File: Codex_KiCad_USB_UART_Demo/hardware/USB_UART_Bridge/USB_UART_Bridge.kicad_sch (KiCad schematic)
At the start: 8 parts, among them J1 USB-C_Receptacle_USB2.0, J2 UART, U2 USBLC6-2SC6

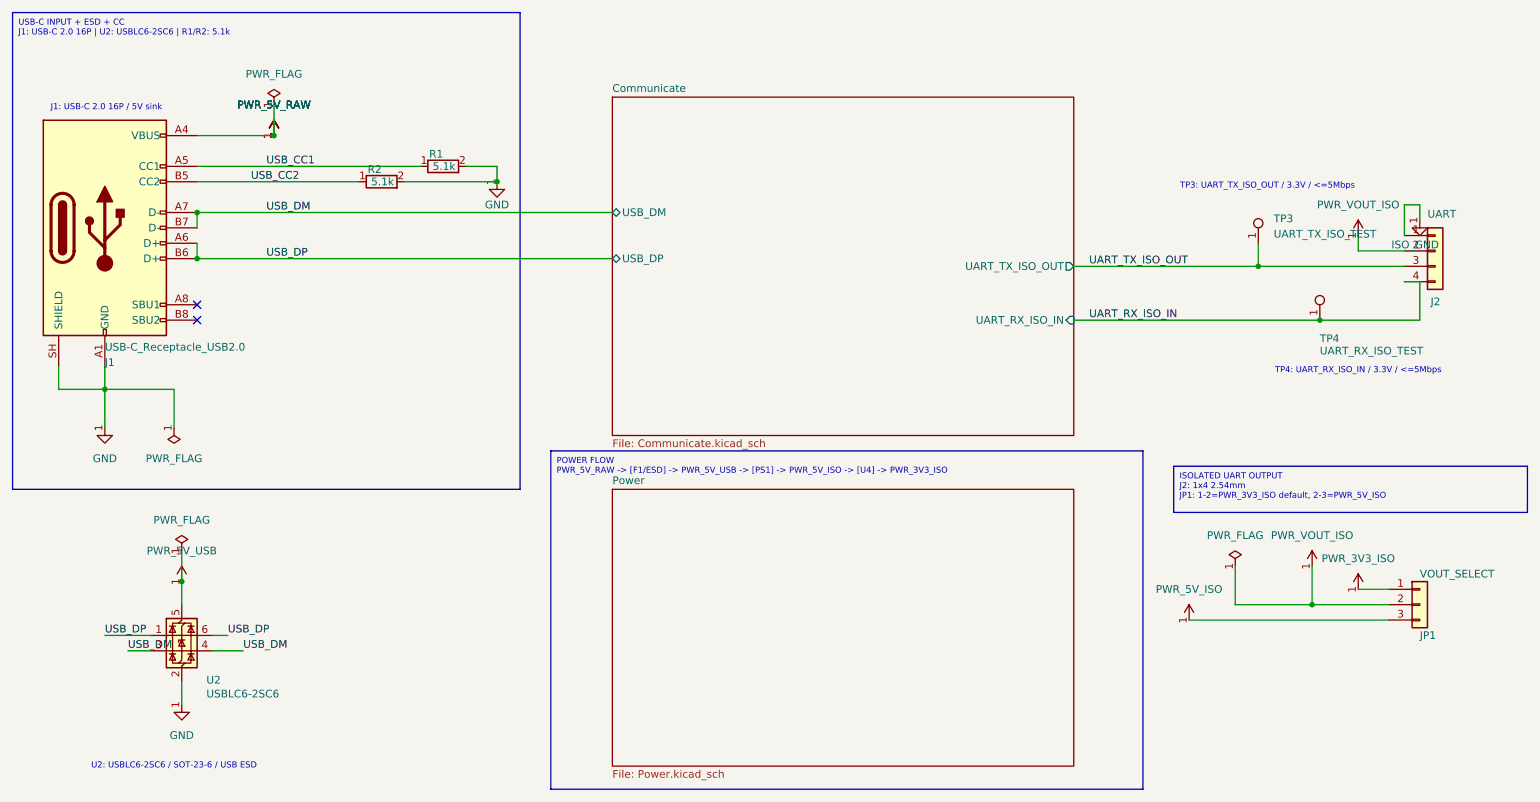
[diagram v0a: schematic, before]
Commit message: feat: complete USB UART PCB layout and routing
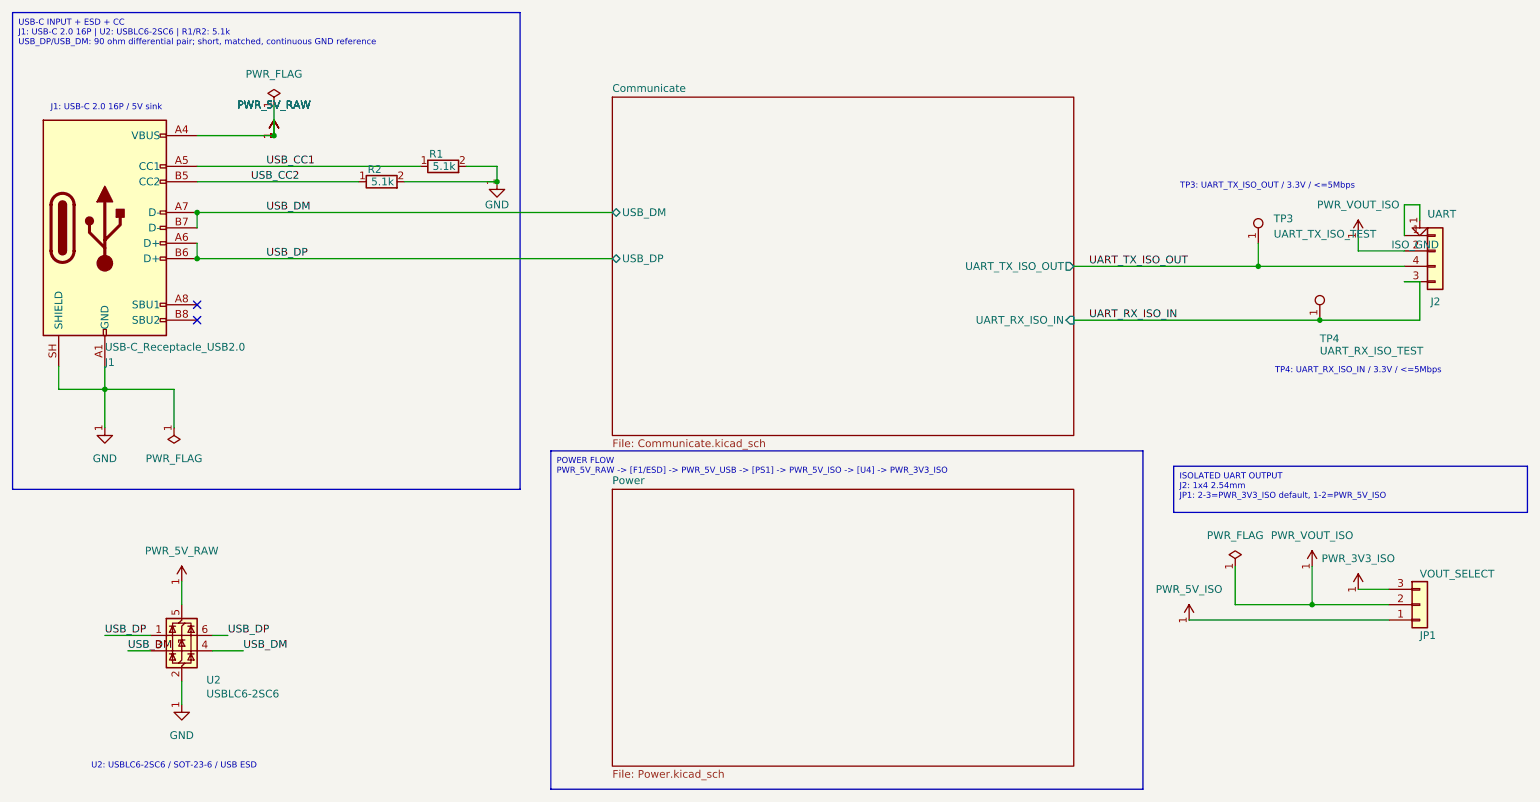
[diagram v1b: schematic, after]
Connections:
- net PWR_5V_USB is gone; now on net PWR_5V_RAW: U2.5 (VBUS)
- net PWR_3V3_ISO: now also JP1.3 (Pin_3); no longer JP1.1 (Pin_1)
- net PWR_5V_ISO: now also JP1.1 (Pin_1); no longer JP1.3 (Pin_3)
- net UART_RX_ISO_IN: now also J2.3 (Pin_3); no longer J2.4 (Pin_4)
- net UART_TX_ISO_OUT: now also J2.4 (Pin_4); no longer J2.3 (Pin_3)
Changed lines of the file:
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@@
 	(title_block
 		(title "USB_UART_Bridge")
+		(date "2026-09-19")
 		(rev "0.2")
-		(date "2026-09-19")
 	)
 	(text "TP3: UART_TX_ISO_OUT / 3.3V / <=5Mbps"
@@
 		)
 	)
-	(text_box "ISOLATED UART OUTPUT\nJ2: 1x4 2.54mm\nJP1: 1-2=PWR_3V3_ISO default, 2-3=PWR_5V_ISO"
+	(text_box "ISOLATED UART OUTPUT\nJ2: 1x4 2.54mm\nJP1: 2-3=PWR_3V3_ISO default, 1-2=PWR_5V_ISO"
 		(exclude_from_sim no)
 		(at 217.17 106.68 0)
@@
 		)
 	)
-	(text_box "USB-C INPUT + ESD + CC\nJ1: USB-C 2.0 16P | U2: USBLC6-2SC6 | R1/R2: 5.1k"
+	(text_box "USB-C INPUT + ESD + CC\nJ1: USB-C 2.0 16P | U2: USBLC6-2SC6 | R1/R2: 5.1k\nUSB_DP/USB_DM: 90 ohm differential pair; short, matched, continuous GND reference"
 		(exclude_from_sim no)
 		(at 25.4 31.75 0)
@@
 	)
 	(junction
-		(at 53.34 125.73)
-		(diameter 0)
-		(color 0 0 0 0)
-	)
-	(junction
 		(at 231.14 73.66)
 		(diameter 0)
@@
 		(pts
 			(xy 100.33 57.15) (xy 105.41 57.15)
-		)
-		(stroke
-			(width 0)
-			(type default)
-		)
-	)
-	(wire
-		(pts
-			(xy 53.34 125.73) (xy 53.34 120.65)
 		)
 		(stroke
@@
 		(instances
 			(project "USB_UART_Bridge"
-				(path "/6d719abe-8294-4a13-afeb-1c2f95178f03"
+				(path "/991ad087-5b84-4353-b5af-12ada82ec90c"
 					(reference "#PWR055")
 					(unit 1)
@@
 		(instances
 			(project "USB_UART_Bridge"
-				(path "/6d719abe-8294-4a13-afeb-1c2f95178f03"
+				(path "/991ad087-5b84-4353-b5af-12ada82ec90c"
 					(reference "#PWR047")
 					(unit 1)
@@
 		(instances
 			(project "USB_UART_Bridge"
-				(path "/6d719abe-8294-4a13-afeb-1c2f95178f03"
+				(path "/991ad087-5b84-4353-b5af-12ada82ec90c"
 					(reference "#PWR046")
 					(unit 1)
@@
 		(instances
 			(project "USB_UART_Bridge"
-				(path "/6d719abe-8294-4a13-afeb-1c2f95178f03"
+				(path "/991ad087-5b84-4353-b5af-12ada82ec90c"
 					(reference "#PWR048")
 					(unit 1)
@@
 		(instances
 			(project "USB_UART_Bridge"
-				(path "/6d719abe-8294-4a13-afeb-1c2f95178f03"
+				(path "/991ad087-5b84-4353-b5af-12ada82ec90c"
 					(reference "#FLG004")
 					(unit 1)
@@
 		(instances
 			(project "USB_UART_Bridge"
-				(path "/6d719abe-8294-4a13-afeb-1c2f95178f03"
+				(path "/991ad087-5b84-4353-b5af-12ada82ec90c"
 					(reference "U2")
 					(unit 1)
@@
 		(instances
 			(project "USB_UART_Bridge"
-				(path "/6d719abe-8294-4a13-afeb-1c2f95178f03"
+				(path "/991ad087-5b84-4353-b5af-12ada82ec90c"
 					(reference "#PWR059")
 					(unit 1)
@@
 		(instances
 			(project "USB_UART_Bridge"
-				(path "/6d719abe-8294-4a13-afeb-1c2f95178f03"
+				(path "/991ad087-5b84-4353-b5af-12ada82ec90c"
 					(reference "#PWR058")
 					(unit 1)
@@
 		(instances
 			(project "USB_UART_Bridge"
-				(path "/6d719abe-8294-4a13-afeb-1c2f95178f03"
+				(path "/991ad087-5b84-4353-b5af-12ada82ec90c"
 					(reference "#FLG003")
 					(unit 1)
@@
 		(instances
 			(project "USB_UART_Bridge"
-				(path "/6d719abe-8294-4a13-afeb-1c2f95178f03"
+				(path "/991ad087-5b84-4353-b5af-12ada82ec90c"
 					(reference "#PWR060")
 					(unit 1)
@@
 		(instances
 			(project "USB_UART_Bridge"
-				(path "/6d719abe-8294-4a13-afeb-1c2f95178f03"
+				(path "/991ad087-5b84-4353-b5af-12ada82ec90c"
 					(reference "#PWR062")
 					(unit 1)
@@
 		(instances
 			(project "USB_UART_Bridge"
-				(path "/6d719abe-8294-4a13-afeb-1c2f95178f03"
+				(path "/991ad087-5b84-4353-b5af-12ada82ec90c"
 					(reference "#PWR052")
 					(unit 1)
@@
 		(instances
 			(project "USB_UART_Bridge"
-				(path "/6d719abe-8294-4a13-afeb-1c2f95178f03"
+				(path "/991ad087-5b84-4353-b5af-12ada82ec90c"
 					(reference "#PWR061")
 					(unit 1)
@@
 		(instances
 			(project "USB_UART_Bridge"
-				(path "/6d719abe-8294-4a13-afeb-1c2f95178f03"
+				(path "/991ad087-5b84-4353-b5af-12ada82ec90c"
 					(reference "J1")
 					(unit 1)
@@
 		(instances
 			(project "USB_UART_Bridge"
-				(path "/6d719abe-8294-4a13-afeb-1c2f95178f03"
+				(path "/991ad087-5b84-4353-b5af-12ada82ec90c"
 					(reference "JP1")
 					(unit 1)
@@
 		(instances
 			(project "USB_UART_Bridge"
-				(path "/6d719abe-8294-4a13-afeb-1c2f95178f03"
+				(path "/991ad087-5b84-4353-b5af-12ada82ec90c"
 					(reference "J2")
 					(unit 1)
@@
 		(instances
 			(project "USB_UART_Bridge"
-				(path "/6d719abe-8294-4a13-afeb-1c2f95178f03"
+				(path "/991ad087-5b84-4353-b5af-12ada82ec90c"
 					(reference "TP3")
 					(unit 1)
@@
 		(instances
 			(project "USB_UART_Bridge"
-				(path "/6d719abe-8294-4a13-afeb-1c2f95178f03"
+				(path "/991ad087-5b84-4353-b5af-12ada82ec90c"
 					(reference "R1")
 					(unit 1)
@@
 		(instances
 			(project "USB_UART_Bridge"
-				(path "/6d719abe-8294-4a13-afeb-1c2f95178f03"
+				(path "/991ad087-5b84-4353-b5af-12ada82ec90c"
 					(reference "#FLG001")
 					(unit 1)
@@
 			)
 		)
-		(property "Value" "PWR_5V_USB"
+		(property "Value" "PWR_5V_RAW"
 			(at 53.34 120.65 0)
 			(show_name no)
@@
 		(instances
 			(project "USB_UART_Bridge"
-				(path "/6d719abe-8294-4a13-afeb-1c2f95178f03"
+				(path "/991ad087-5b84-4353-b5af-12ada82ec90c"
 					(reference "#PWR049")
 					(unit 1)
@@
 		(instances
 			(project "USB_UART_Bridge"
-				(path "/6d719abe-8294-4a13-afeb-1c2f95178f03"
+				(path "/991ad087-5b84-4353-b5af-12ada82ec90c"
 					(reference "#PWR056")
-					(unit 1)
-				)
-			)
-		)
-	)
-	(symbol
-		(lib_id "power:PWR_FLAG")
-		(at 53.34 120.65 0)
-		(unit 1)
-		(body_style 1)
-		(exclude_from_sim no)
-		(in_bom yes)
-		(on_board yes)
-		(in_pos_files yes)
-		(dnp no)
-		(property "Reference" "#FLG002"
-			(at 53.34 122.555 0)
-			(hide yes)
-			(show_name no)
-			(do_not_autoplace no)
-			(effects
-				(font
-					(size 1.27 1.27)
-				)
-				(justify left)
-			)
-		)
-		(property "Value" "PWR_FLAG"
-			(at 53.34 115.57 0)
-			(show_name no)
-			(do_not_autoplace no)
-			(effects
-				(font
-					(size 1.27 1.27)
-				)
-			)
-		)
-		(property "Footprint" ""
-			(at 53.34 120.65 0)
-			(show_name no)
-			(do_not_autoplace no)
-			(effects
-				(font
-					(size 1.27 1.27)
-				)
-			)
-		)
-		(property "Datasheet" ""
-			(at 53.34 120.65 0)
-			(show_name no)
-			(do_not_autoplace no)
-			(effects
-				(font
-					(size 1.27 1.27)
-				)
-			)
-		)
-		(property "Description" ""
-			(at 53.34 120.65 0)
-			(show_name no)
-			(do_not_autoplace no)
-			(effects
-				(font
-					(size 1.27 1.27)
-				)
-			)
-		)
-		(pin "1"
-		)
-		(instances
-			(project "USB_UART_Bridge"
-				(path "/6d719abe-8294-4a13-afeb-1c2f95178f03"
-					(reference "#FLG002")
 					(unit 1)
 				)
@@
 		(instances
 			(project "USB_UART_Bridge"
-				(path "/6d719abe-8294-4a13-afeb-1c2f95178f03"
+				(path "/991ad087-5b84-4353-b5af-12ada82ec90c"
 					(reference "TP4")
 					(unit 1)
@@
 		(instances
 			(project "USB_UART_Bridge"
-				(path "/6d719abe-8294-4a13-afeb-1c2f95178f03"
+				(path "/991ad087-5b84-4353-b5af-12ada82ec90c"
 					(reference "#PWR045")
 					(unit 1)
@@
 		(instances
 			(project "USB_UART_Bridge"
-				(path "/6d719abe-8294-4a13-afeb-1c2f95178f03"
+				(path "/991ad087-5b84-4353-b5af-12ada82ec90c"
 					(reference "R2")
 					(unit 1)
@@
 		(instances
 			(project "USB_UART_Bridge"
-				(path "/6d719abe-8294-4a13-afeb-1c2f95178f03"
+				(path "/991ad087-5b84-4353-b5af-12ada82ec90c"
 					(page "2")
 				)
@@
 		(instances
 			(project "USB_UART_Bridge"
-				(path "/6d719abe-8294-4a13-afeb-1c2f95178f03"
+				(path "/991ad087-5b84-4353-b5af-12ada82ec90c"
 					(page "3")
 				)
